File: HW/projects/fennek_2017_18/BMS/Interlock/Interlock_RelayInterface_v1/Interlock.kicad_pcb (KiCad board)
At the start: 2 copper layers, 41 x 24.5 mm, 34 parts, among them K1 ASSR-1218, K2 ASSR-1218, K3 ASSR-1218, P1 12V, P2 crtl, P3 IL1, P4 IL2, U1 TMR_1-1212

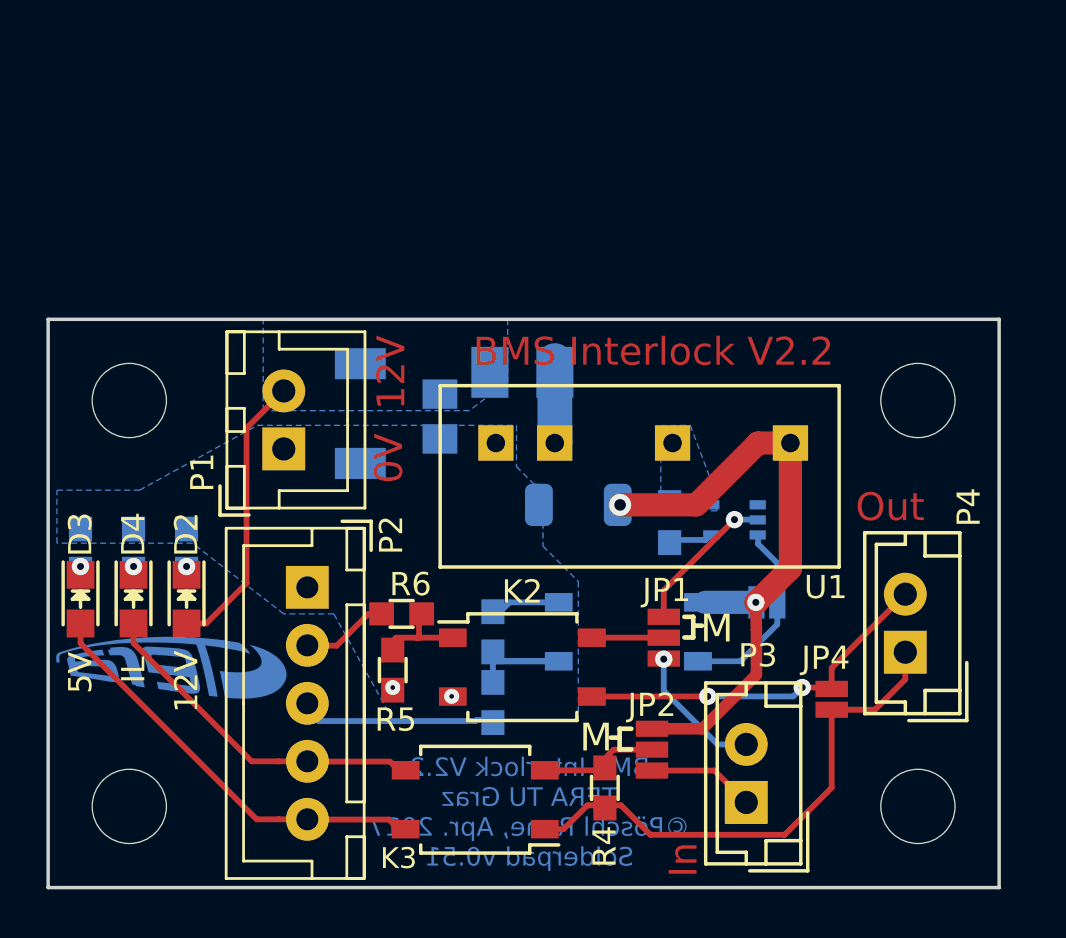
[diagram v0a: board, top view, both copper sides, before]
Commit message: Update github repo with designs for fennek 2018
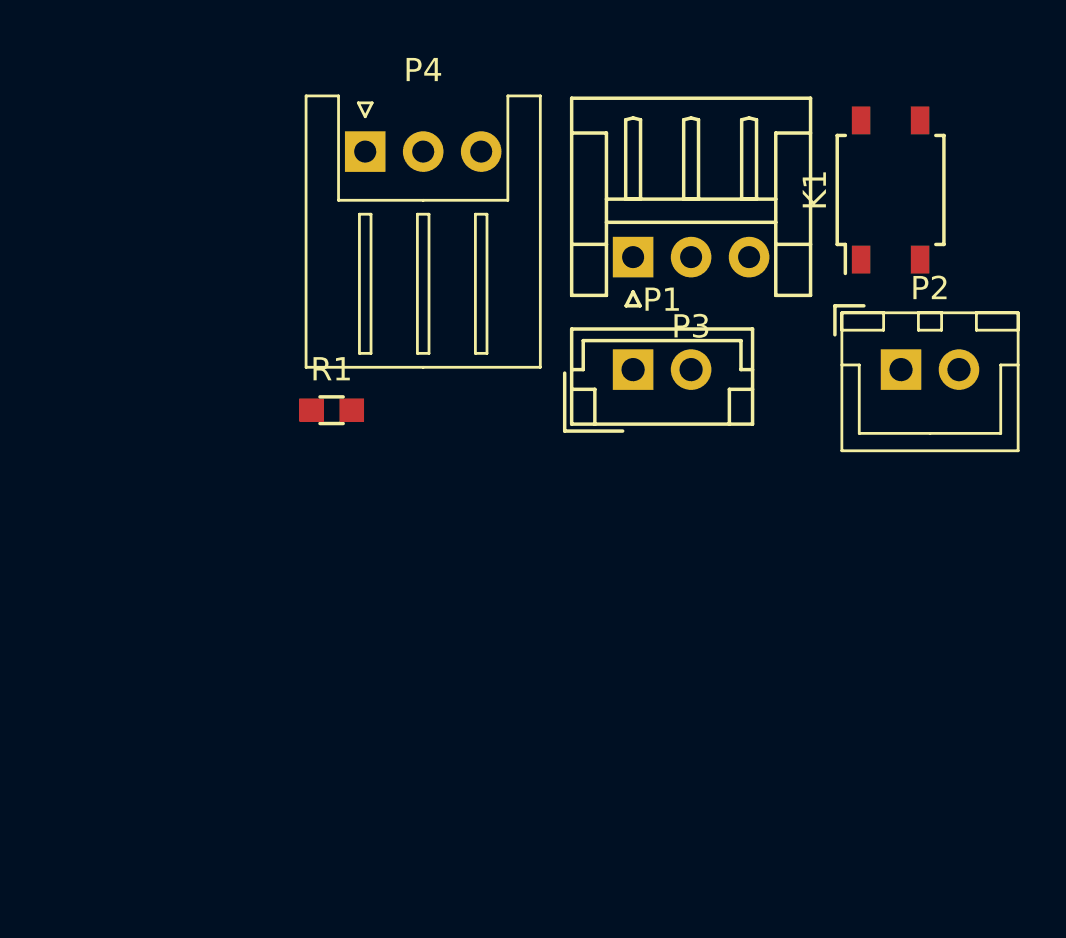
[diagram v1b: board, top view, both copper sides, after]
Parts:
- removed C1: 4.7uF 25V, tera_rlc:C_0805in
- removed C2: 220pF 2kV, tera_rlc:C_1206in_HV
- removed D1: 18V, tera_diodes:DO-214AA
- removed D2: 12V_OK, tera_diodes:LED_0805
- removed D3: VDD_OK, tera_diodes:LED_0805
- removed D4: IL_OK, tera_diodes:LED_0805
- removed G1: PSSI2021SAY, tera_atomic_ic:PSSI2021SAY
- removed JP1, JP2: first/middle, tera_general:SOLDERJUMPER_3
- removed JP3: I_sup_on, tera_general:SOLDERJUMPER_2
- removed JP4: Last In Line, tera_general:SOLDERJUMPER_2
- removed K2, K3: ASSR-1218, tera_general:SO-4
- removed L1: 4.7uH 1.2A, tera_rlc:L_muarta_LQH32PN
- removed R2, R4, R5: 1K, tera_rlc:R_0603in
- removed R3: 120R, tera_rlc:R_0603in
- removed R6: 470, tera_rlc:R_0603in
- removed R7: 12k, tera_rlc:R_0603in
- removed R8, R9: 5k1, tera_rlc:R_0603in
- removed REF** (x4): MountingHole_3.2mm_M3, Mounting_Holes:MountingHole_3.2mm_M3
- removed U1: TMR_1-1212, traco_power:TMR_1-XX1X
- removed svg2mod: G***, tera_logos:TERA_TextOnly_Cu_2.5x9.5mm
- K1: moved to F.Cu
- P1: value 12V -> IL1; footprint tera_Connectors_JST:JST_XH_B02B-XH-A_02x2.50mm_Straight -> tera_Connectors_JST:JST_EH_B02B-EH-A_02x2.50mm_Straight
- P2: value crtl -> Relay_in; footprint tera_Connectors_JST:JST_XH_B05B-XH-A_05x2.50mm_Straight -> tera_Connectors_JST:JST_XH_B02B-XH-A_02x2.50mm_Straight
- P3: value IL1 -> IL2; footprint tera_Connectors_JST:JST_EH_B02B-EH-A_02x2.50mm_Straight -> tera_Connectors_JST:JST_EH_S03B-EH_03x2.50mm_Angled
- P4: value IL2 -> Relay_out; footprint tera_Connectors_JST:JST_EH_B02B-EH-A_02x2.50mm_Straight -> tera_Connectors_JST:JST_XH_S03B-XH-A_03x2.50mm_Angled
- R1: value 470 -> 1K; moved to F.Cu
- moved P4 31.8 mm to (69.2, 80.8), turned to 0 degrees
- moved P2 27.3 mm to (92.3, 90.2), turned to 0 degrees
- moved P3 24.0 mm to (80.7, 85.3), turned to 0 degrees
- moved K1 22.2 mm to (91.8, 82.4), turned to 0 degrees
- moved P1 15.4 mm to (80.7, 90.2), turned to 0 degrees
- moved R1 14.4 mm to (67.7, 91.9), turned to 0 degrees
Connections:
- K1 pad 2: GND -> Net-(K1-Pad2)
- K1 pad 3: IL_V- -> Net-(K1-Pad3)
- K1 pad 4: Net-(G1-Pad3) -> Net-(K1-Pad4)
- P1 pad 1: GND -> Net-(K1-Pad2)
- P1 pad 2: +12V -> Net-(P1-Pad2)
- P2 pad 1: GND -> Net-(K1-Pad3)
- P2 pad 2: /IL_OUT_OK -> Net-(P2-Pad2)
- P3 pad 1: /IL_In- -> Net-(K1-Pad1)
- P3 pad 2: /IL_In+ -> Net-(P3-Pad2)
- P4 pad 1: /IL_Out- -> Net-(K1-Pad4)
- P4 pad 2: /IL_Out+ -> Net-(P4-Pad2)
- R1 pad 2: /IL_I_ON -> Net-(K1-Pad2)
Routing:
- net IL_V-: track 26.6 -> 0.00 mm, vias 2 -> 0
- net /IL_Out-: track 22.3 -> 0.00 mm
- net VDD: track 18.1 -> 0.00 mm
- net /IL_Out+: track 15.6 -> 0.00 mm, vias 2 -> 0
- net /IL_in_OK: track 14.8 -> 0.00 mm
- net +12V: track 12.3 -> 0.00 mm
- net /IL_I_ON: track 8.59 -> 0.00 mm
- net Net-(G1-Pad3): track 7.99 -> 0.00 mm
- net Net-(K1-Pad1): track 6.80 -> 0.00 mm
- net /IL_Iconst: track 6.47 -> 0.00 mm, vias 1 -> 0
- net /IL_In+: track 5.90 -> 0.00 mm, vias 1 -> 0
- net Net-(JP2-Pad2): track 5.00 -> 0.00 mm
- net /IL_In-: track 4.63 -> 0.00 mm
- net /IL_OUT_OK: track 4.14 -> 0.00 mm
- net Net-(K2-Pad1): track 3.88 -> 0.00 mm
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- removed copper zone on B.Cu, net +12V
- removed copper zone on B.Cu, net GND
- removed copper zone on B.Cu, net IL_V+
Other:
- board outline removed
- board text removed: "0V"
- board text removed: "12V"
- board text removed: "5V"
- board text removed: "BMS Interlock V2.2"
- board text removed: "BMS Interlock V2.2 TERA TU Graz ©Pöschl Rene, Apr. 2017 Solderpad v0.51"
- board text removed: "IL"
- board text removed: "In"
- board text removed: "M"
- board text removed: "Out"
